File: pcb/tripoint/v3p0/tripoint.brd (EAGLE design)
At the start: 31.8 x 27.5 mm, 43 parts, among them T1 HHM1595A1, U1 STM32F091CC, U2 DW1000, U3 SKY13317, U4 LXDC2HN18A, X1 38.4M, X2 16M

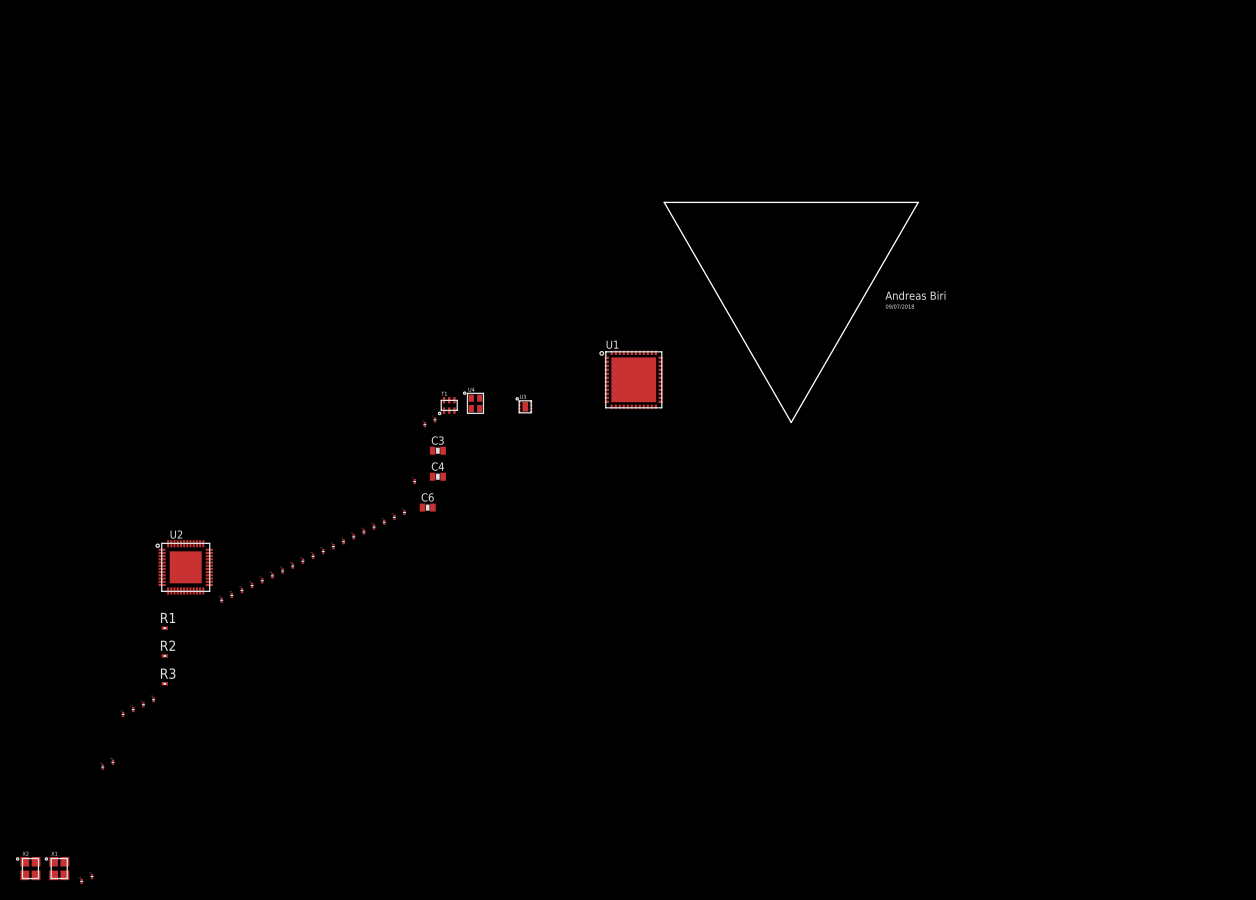
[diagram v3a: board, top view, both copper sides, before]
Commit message: finished first draft of schematic
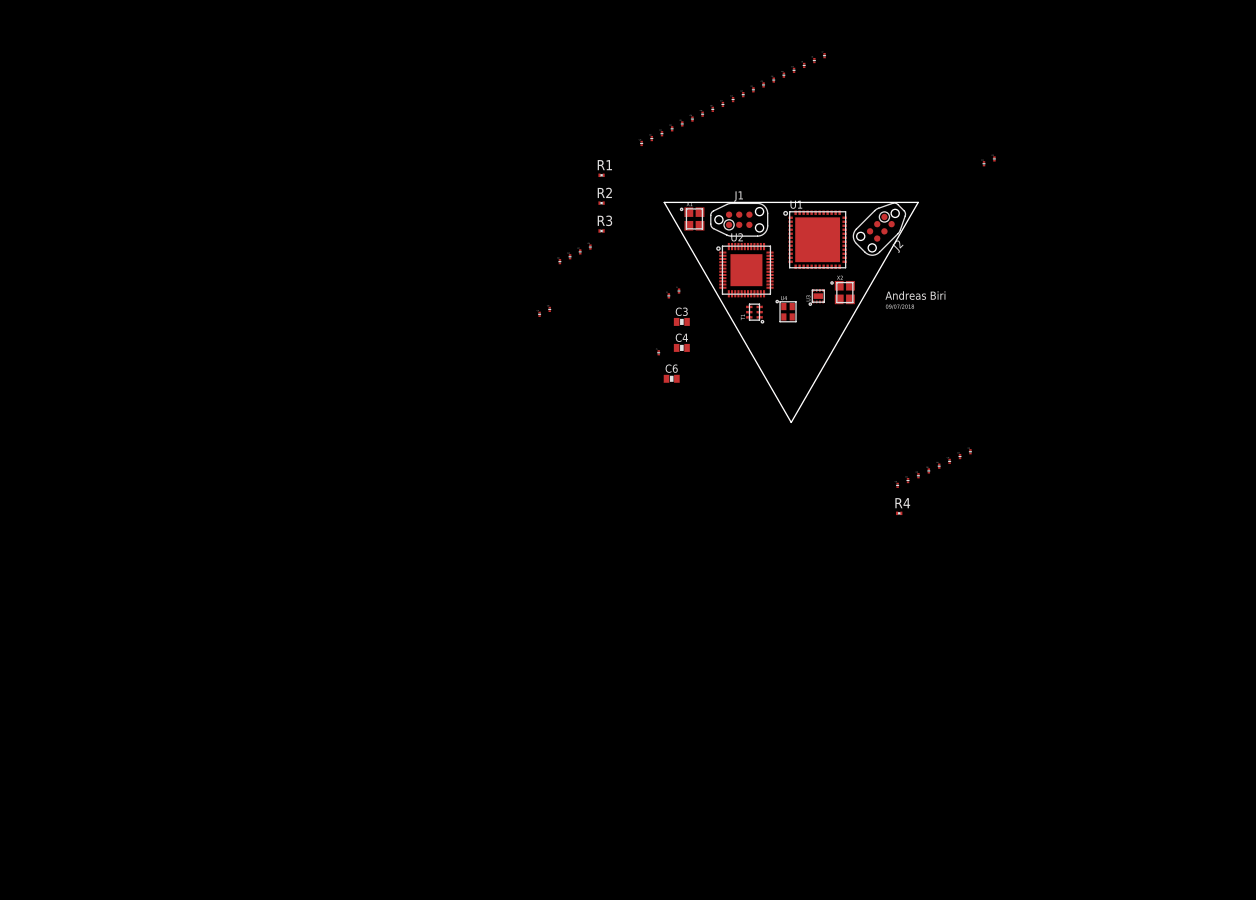
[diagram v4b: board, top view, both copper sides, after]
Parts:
- added C34, C35, C36, C38: 100nF, passives:0201_CAP
- added C37, C39: 4.7uF, passives:0201_CAP
- added C40: 10nF, passives:0201_CAP
- added C41: 1uF, passives:0201_CAP
- added J1, J2: TC2030-JLINK-NL, connector:TC2030-IDC-NL
- added R4: 11k, rcl:R0201
- C30, C31: value 8.5pF -> 12pF
- C32, C33: value 8pF -> 12pF
- moved C33 144.1 mm to (24.1, 14.0)
- moved C32 144.1 mm to (25.4, 14.6)
- moved X2 124.7 mm to (6.70, -2.10)
- moved X1 113.6 mm to (-12.1, 7.10)
- moved U2 79.3 mm to (-5.60, 0.70)
- moved C26 78.6 mm to (-25.1, 3.59)
- moved C30 78.6 mm to (-30.2, -4.21)
- moved C27 78.6 mm to (-26.4, 2.98)
- moved C28 78.6 mm to (-27.6, 2.37)
- moved C29 78.6 mm to (-28.9, 1.76)
- moved C31 78.6 mm to (-31.5, -4.82)
- moved R2 78.6 mm to (-23.7, 9.08)
- moved R3 78.6 mm to (-23.7, 5.60)
- moved R1 78.6 mm to (-23.7, 12.6)
- moved C11 77.6 mm to (-0.92, 25.1)
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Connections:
- removed net VBAT: U1.1
- removed net VDD/24: U1.24
- removed net VDD/48: U1.48
- removed net VDDA: U1.9
- removed net VDDIO2: U1.36
- removed net VSS/23: U1.23
- removed net VSS/35: U1.35
- removed net VSS/47: U1.47
- removed net VSSA: U1.8
- new net !SPI1_SS: U1.14
- new net !STM_RST: J2.3, U1.7
- new net +3V3: J2.1, U1.1, U1.24, U1.36, U1.48, U1.9
- new net GPIO0: J1.3, U1.42
- new net GPIO1: J1.6, U1.43
- new net GPIO2: J1.4, U1.45
- new net GPIO3: J1.2, U1.46
- new net GPIO4: J1.1, U1.21
- new net GPIO5: J1.5, U1.22
- new net I2C1_SCL: U1.30
- new net I2C1_SDA: U1.31
- new net INTERRUPT: U1.13
- new net N$8: R4.1, U1.44
- new net SPI1_MISO: U1.16
- new net SPI1_MOSI: U1.17
- new net STM_SWCLK: J2.4, U1.37
- new net STM_SWDIO: J2.2, U1.34
- net !DW_RST: now also U1.18
- net ANT_SEL1: now also U1.39
- net ANT_SEL2: now also U1.40
- net ANT_SEL3: now also U1.41
- net DW_IRQ: now also U1.20
- net DW_WAKEUP: now also U1.19
- net GND: now also C34.P$2, C35.P$2, C36.P$2, C37.P$2, C38.P$2, C39.P$2, C40.P$2, C41.P$2, J2.5, R4.2, U1.23, U1.35, U1.47, U1.8
- net SPI_CLK: now also U1.15
- net V3P3: now also C34.P$1, C35.P$1, C36.P$1, C37.P$1, C38.P$1, C39.P$1, C40.P$1, C41.P$1

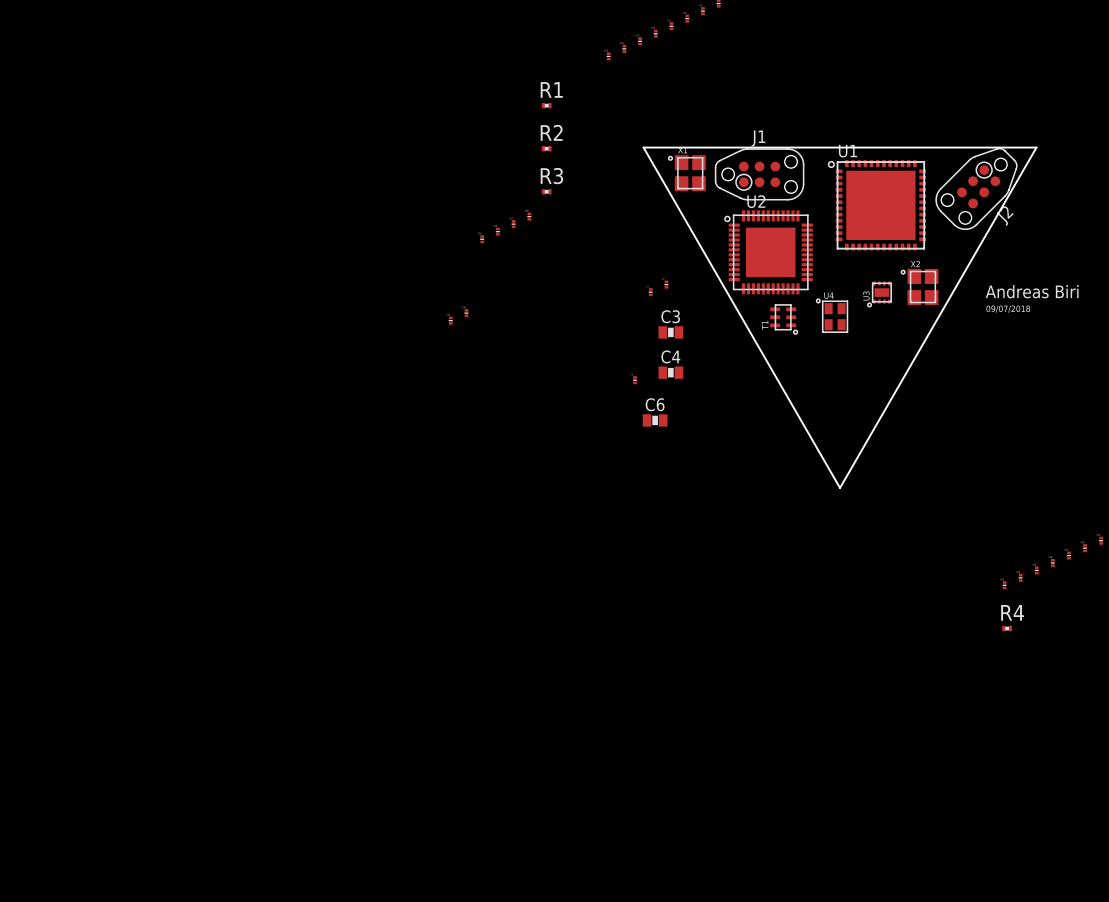
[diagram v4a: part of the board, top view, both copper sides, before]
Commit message: added LED, test pads, external signals and Lab11 power symbols
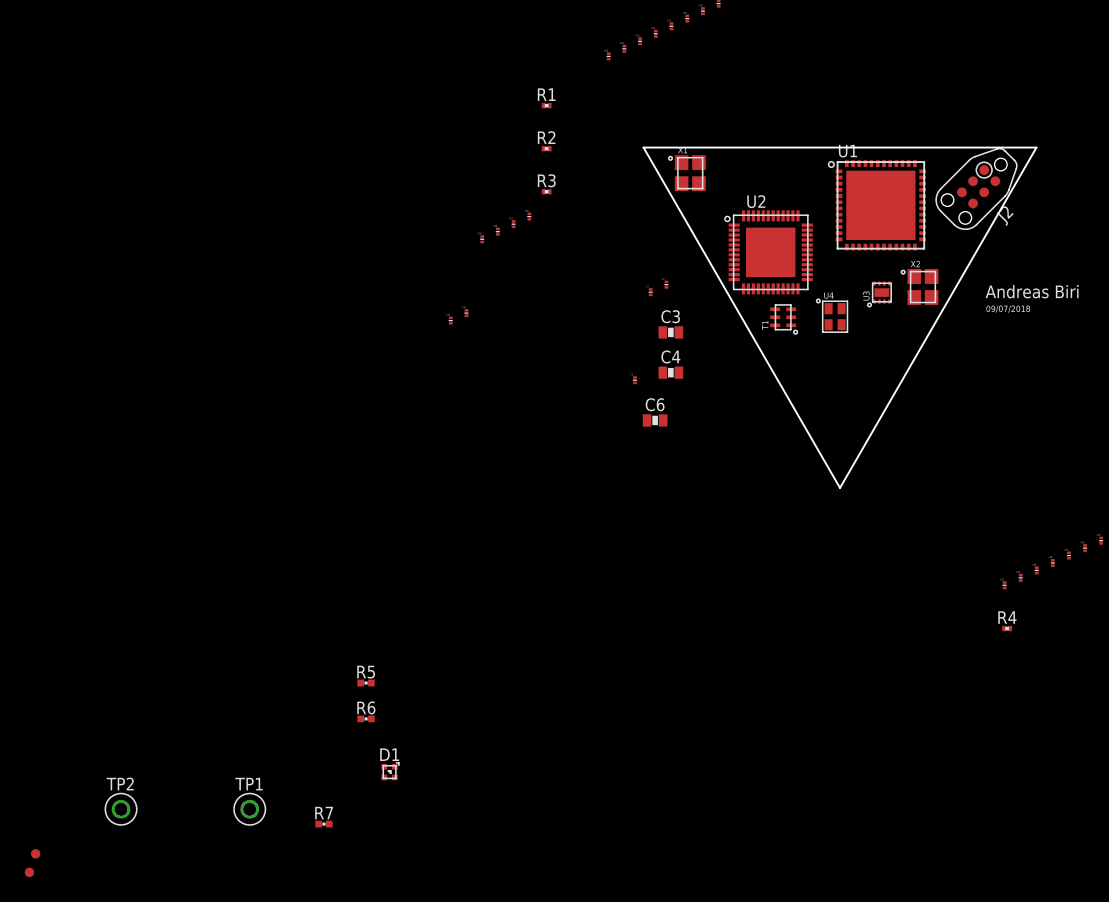
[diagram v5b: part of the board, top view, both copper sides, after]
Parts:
- removed J1: TC2030-JLINK-NL, connector:TC2030-IDC-NL
- added D1: SML-LX0404SIUPGUSB, leds:1MM_SQ_4PAD
- added R5, R6, R7: 1k, passives:0402_RES
- added TP1, TP2: TEST_POINT_0.040IN, headers:TESTPOINT_0.040IN
- added TP3, TP4: TEST-POINT, headers:PAD.03X.03
- R1, R2, R3, R4: device rcl:R0201 -> passives:0201_RES
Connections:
- net I2C1_SCL renamed EXT_I2C_SCL
- net I2C1_SDA renamed EXT_I2C_SDA
- net SPI_CLK renamed DW_SPI_CLK
- net V1P8 renamed 1V8
- net V1P8_EN renamed REG_EN
- net V3P3 renamed 3V3
- removed net !SPI1_SS: U1.14
- removed net !SPI_CS: U2.24
- removed net GPIO4: J1.1, U1.21
- removed net GPIO5: J1.5, U1.22
- removed net SPI1_MISO: U1.16
- removed net SPI1_MOSI: U1.17
- removed net SPI_MISO: U2.40
- removed net SPI_MOSI: U2.39
- new net !DW_SPI_CS: U1.14, U2.24
- new net DW_SPI_MISO: U1.16, U2.40
- new net DW_SPI_MOSI: U1.17, U2.39
- new net LED_BLUE: R7.2, U1.25
- new net LED_GREEN: R6.2, U1.26
- new net LED_RED: R5.2, U1.27
- new net N$10: D1.4, R6.1
- new net N$11: D1.3, R7.1
- new net N$12: D1.2, R5.1
- net +3V3: now also D1.1
- net GPIO0: now also TP1.TESTPOINT; no longer J1.3
- net GPIO1: now also TP2.TESTPOINT; no longer J1.6
- net GPIO2: now also TP3.P$1, U1.21; no longer J1.4, U1.45
- net GPIO3: now also TP4.P$1, U1.22; no longer J1.2, U1.46
- net INTERRUPT: now also U1.12; no longer U1.13

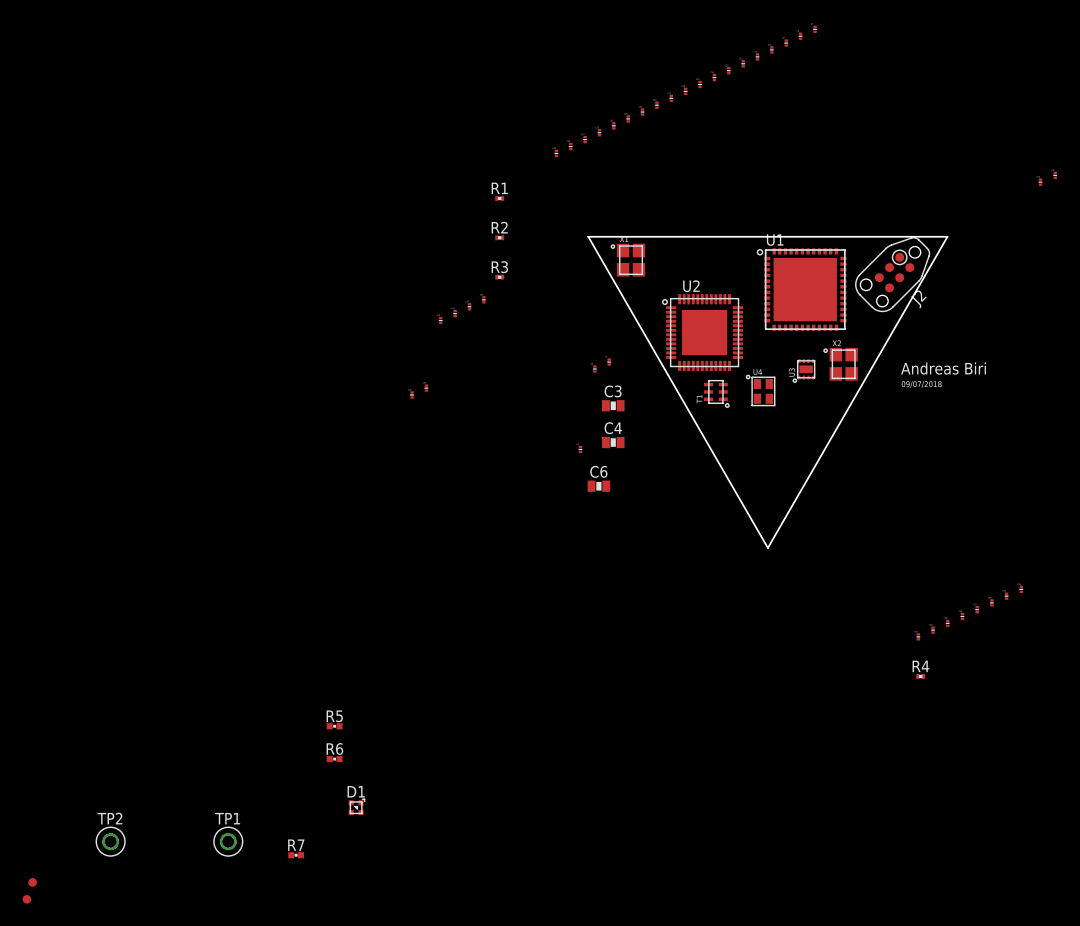
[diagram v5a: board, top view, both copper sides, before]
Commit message: placed major components & RF traces
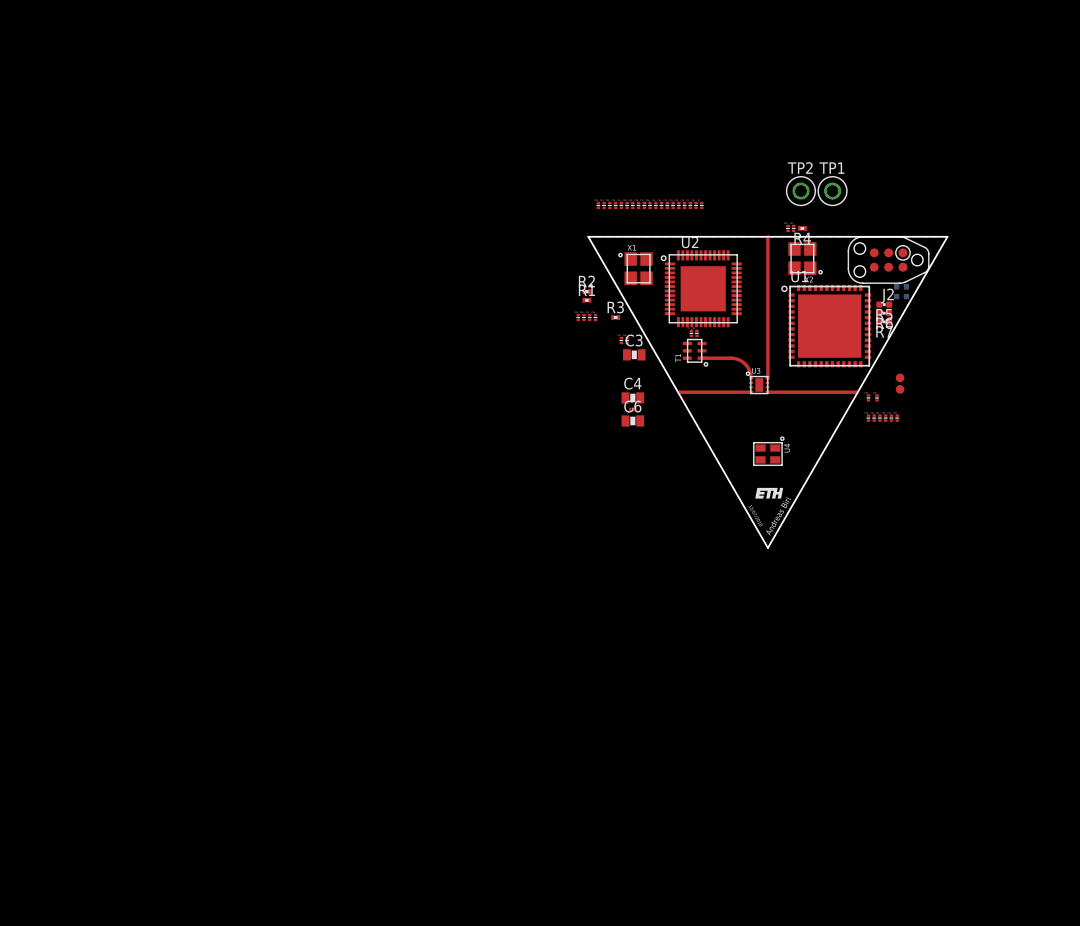
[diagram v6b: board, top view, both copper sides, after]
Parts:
- added U$1: (no value), logos:ETH_100MIL
- moved TP4 89.4 mm to (11.7, -4.32)
- moved TP3 88.7 mm to (11.7, -3.30)
- moved TP2 83.8 mm to (2.92, 13.2)
- moved TP1 78.5 mm to (5.71, 13.2)
- moved R7 70.2 mm to (10.3, 1.65), turned to 180 degrees
- moved D1 66.4 mm to (11.8, 4.32), flipped to the bottom, turned to 270 degrees
- moved R6 62.6 mm to (10.3, 2.41), turned to 180 degrees
- moved R5 61.2 mm to (10.3, 3.17), turned to 180 degrees
- moved R4 41.0 mm to (3.05, 9.91), turned to 180 degrees
- moved C40 37.8 mm to (1.78, 9.91)
- moved C41 37.7 mm to (2.29, 9.91)
- moved C32 25.2 mm to (9.65, -5.08)
- moved C33 24.4 mm to (8.89, -5.08)
- moved C39 19.4 mm to (8.89, -6.86)
- moved C38 19.2 mm to (9.40, -6.86)
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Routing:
- net RF3: track 0.00 -> 12.5 mm
- net RF2: track 0.00 -> 7.93 mm
- net RF1: track 0.00 -> 6.40 mm
- net N$1: track 0.00 -> 5.07 mm
- added copper zone on layer 1, net GND
- added copper zone on layer 2, net GND
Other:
- board text added: "12/07/2018"
- board text removed: "09/07/2018"

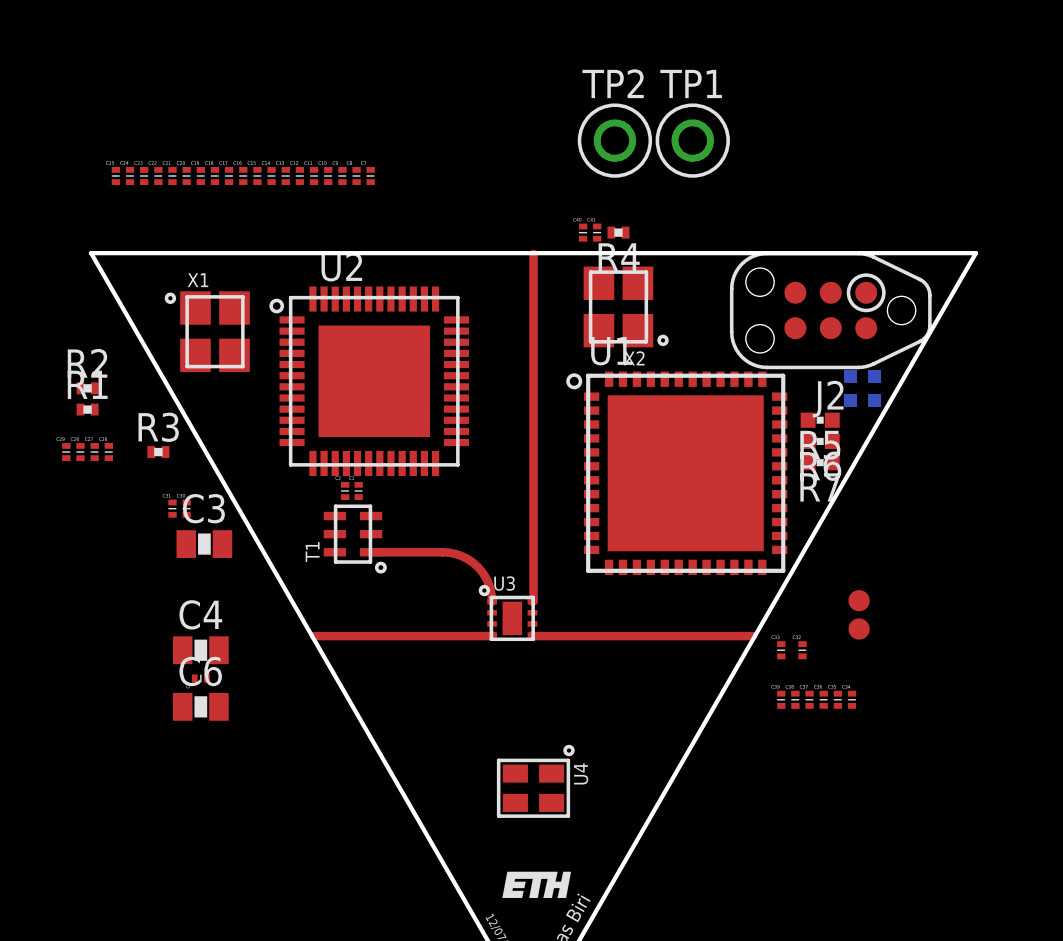
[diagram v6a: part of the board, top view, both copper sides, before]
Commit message: corrected decoupling cap values, added correct res for DEEPSLEEP plus missing decoupling caps
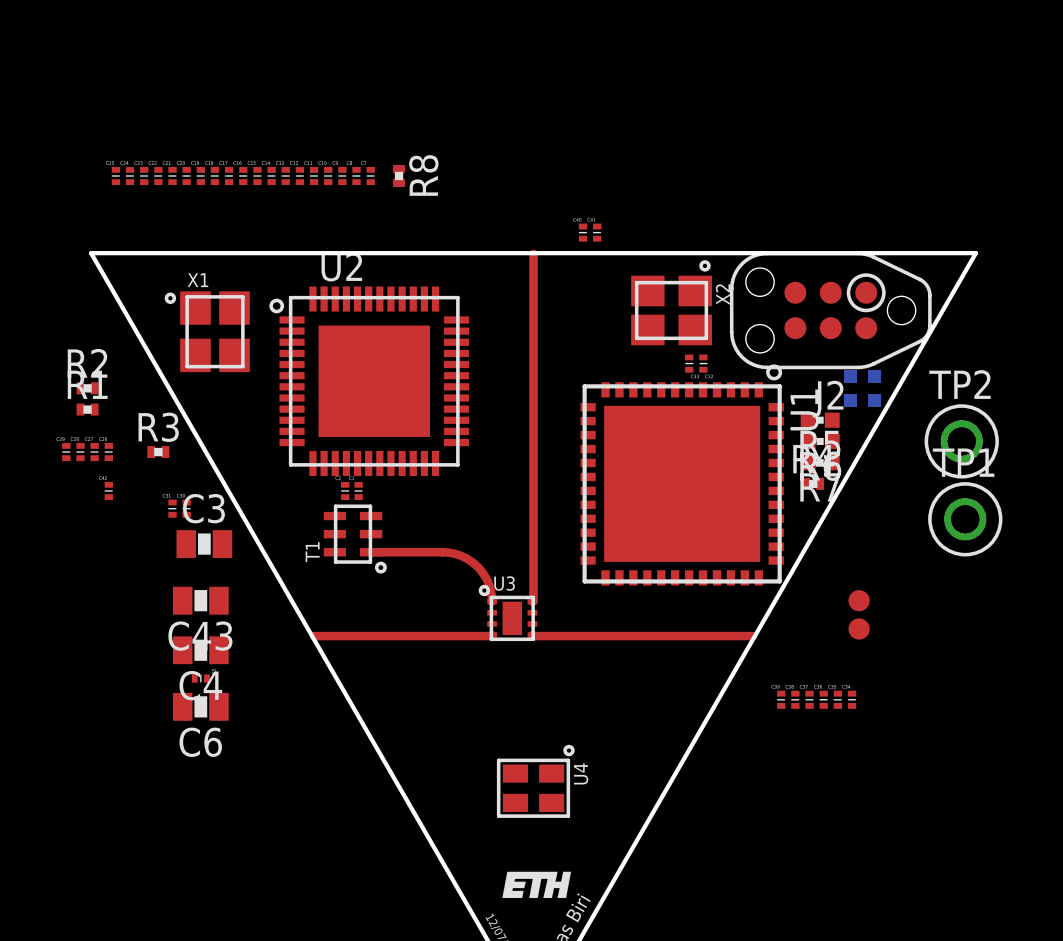
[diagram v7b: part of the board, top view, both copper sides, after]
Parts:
- added C42: 0.1uF, passives:0201_CAP
- added C43: 4.7uF, passives:0603_CAP
- added R8: 100k, passives:0201_RES
- C8: value 100pF -> 0.1uF
- moved TP1 16.7 mm to (15.5, -0.38)
- moved TP2 16.5 mm to (15.4, 2.41)
- moved R4 11.4 mm to (10.0, 0.89), turned to 0 degrees
- moved C32 10.9 mm to (6.10, 5.21), turned to 180 degrees
- moved C33 10.8 mm to (5.59, 5.21), turned to 180 degrees
- moved X2 1.91 mm to (4.95, 7.11), turned to 270 degrees
- moved U1 0.40 mm to (5.33, 0.89), turned to 270 degrees
- turned C4 to 180 degrees
- turned C5 to 270 degrees
- turned C6 to 180 degrees
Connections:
- net 3V3: now also C43.1
- net DW_IRQ: now also R8.2
- net GND: now also C42.P$2, C43.2, R8.1
- net VDDIO: now also C42.P$1
